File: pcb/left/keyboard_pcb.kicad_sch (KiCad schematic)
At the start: 27 parts, among them J1 TRRS, K00 KEYSW, K01 KEYSW, K02 KEYSW, K03 KEYSW, K04 KEYSW, K05 KEYSW, K10 KEYSW, K11 KEYSW, K12 KEYSW, K13 KEYSW, K14 KEYSW, K15 KEYSW, K20 KEYSW, K21 KEYSW, K22 KEYSW, K23 KEYSW, K24 KEYSW, K25 KEYSW, K30 KEYSW, K31 KEYSW, K32 KEYSW, U1 Helios

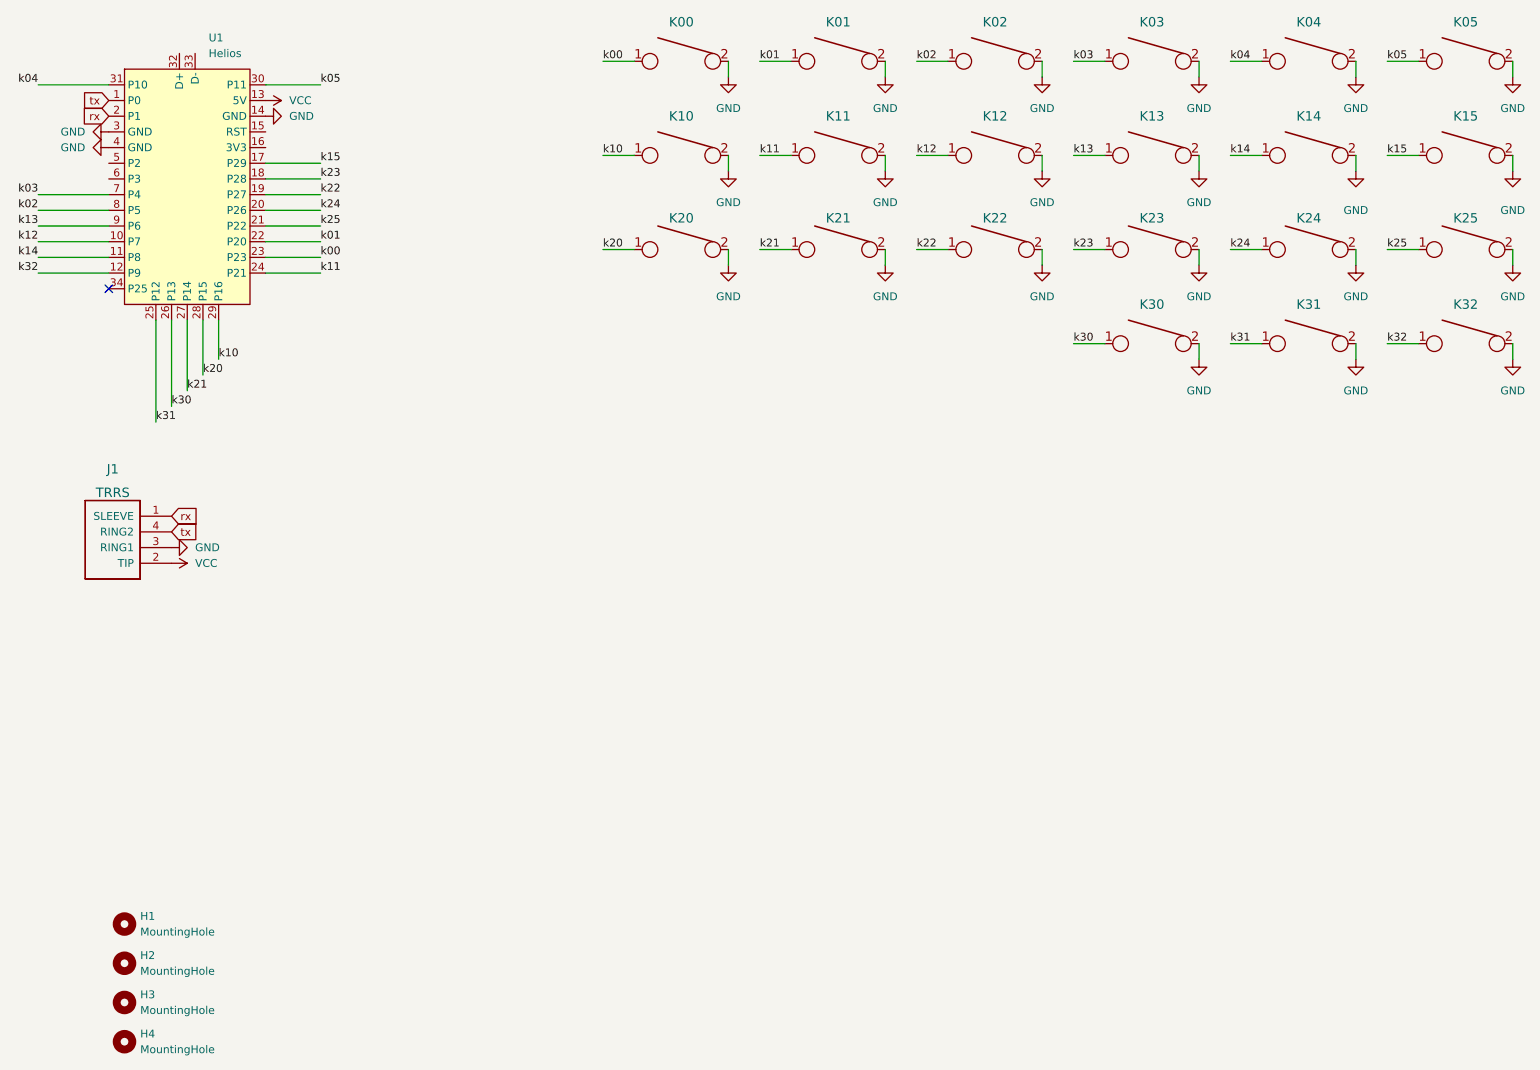
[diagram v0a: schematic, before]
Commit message: Add ground plane. Add reset pins.
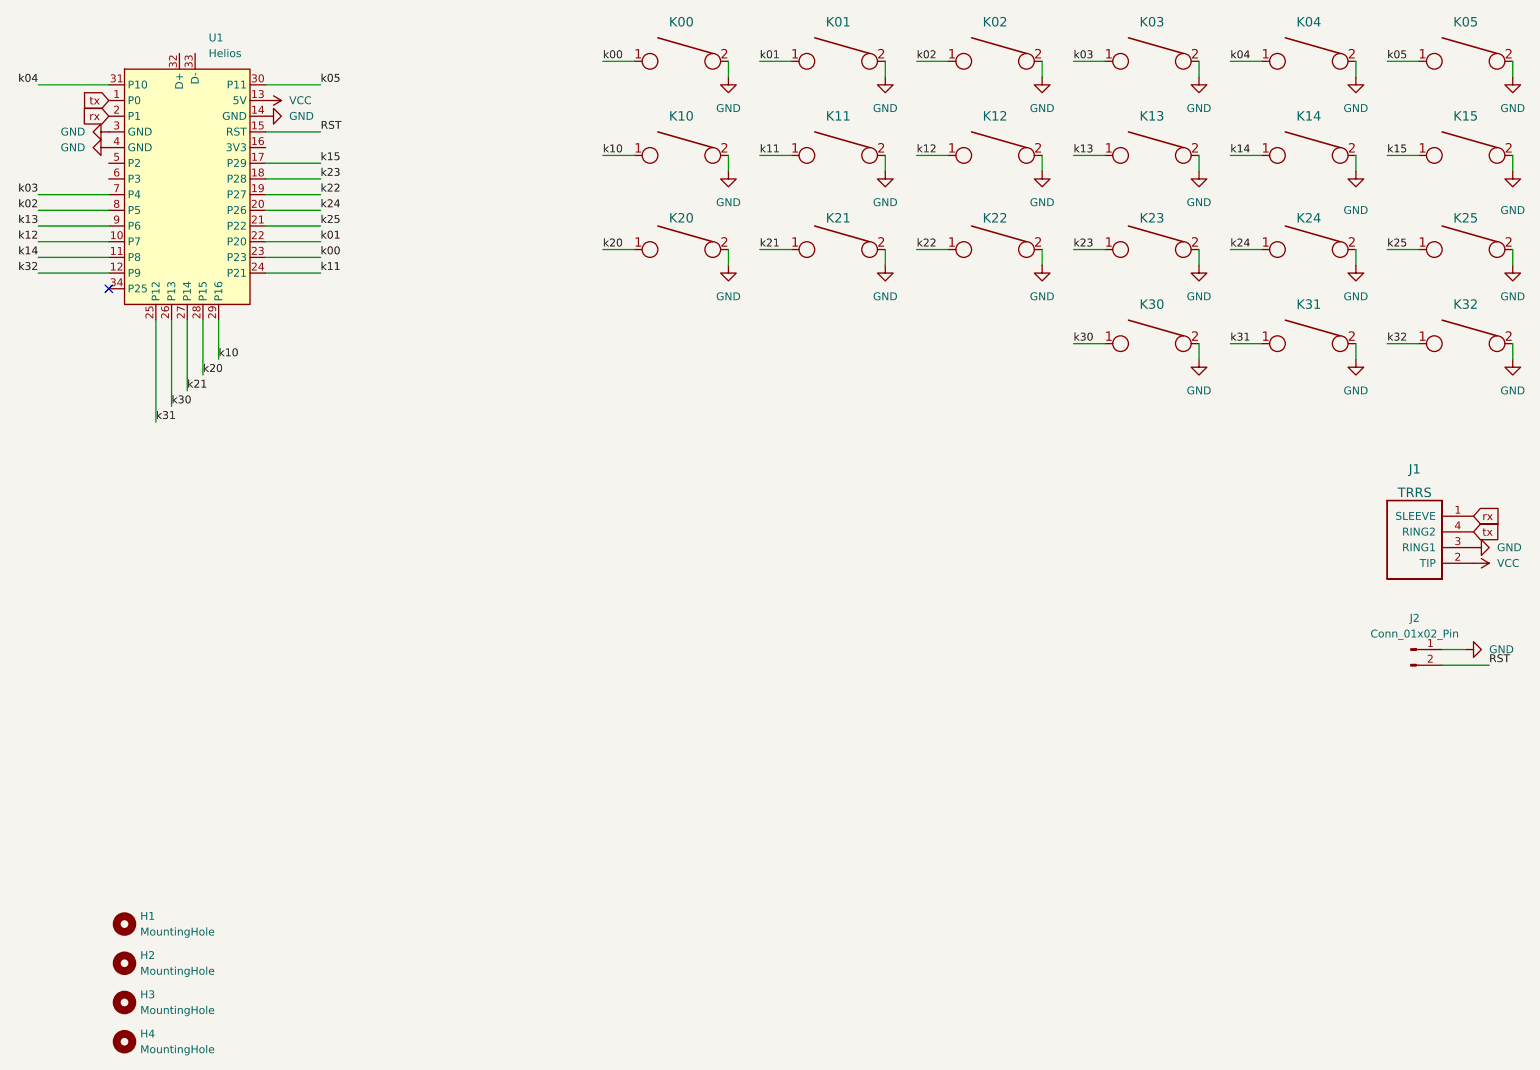
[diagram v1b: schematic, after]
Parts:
- added J2: Conn_01x02_Pin, Connector_PinHeader_2.54mm:PinHeader_1x02_P2.54mm_Vertical, symbol Connector:Conn_01x02_Pin
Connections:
- net GND: now also J2.1 (Pin_1)
- net RST: now reaches U1.15 (RST)
- net RST: now also J2.2 (Pin_2)
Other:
- moved on the sheet: J1
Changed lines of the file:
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@@
 	(wire
 		(pts
+			(xy 69.85 41.91) (xy 78.74 41.91)
+		)
+		(stroke
+			(width 0)
+			(type default)
+		)
+	)
+	(wire
+		(pts
 			(xy 170.18 48.26) (xy 170.18 45.72)
 		)
@@
 	(wire
 		(pts
+			(xy 260.35 125.73) (xy 264.16 125.73)
+		)
+		(stroke
+			(width 0)
+			(type default)
+		)
+	)
+	(wire
+		(pts
 			(xy 33.02 62.23) (xy 44.45 62.23)
 		)
@@
 	(wire
 		(pts
+			(xy 260.35 128.27) (xy 267.97 128.27)
+		)
+		(stroke
+			(width 0)
+			(type default)
+		)
+	)
+	(wire
+		(pts
 			(xy 33.02 54.61) (xy 44.45 54.61)
 		)
@@
 		)
 	)
+	(label "RST"
+		(at 78.74 41.91 0)
+		(fields_autoplaced yes)
+		(effects
+			(font
+				(size 1.27 1.27)
+			)
+			(justify left bottom)
+		)
+	)
 	(label "k24"
 		(at 78.74 54.61 0)
@@
 		)
 	)
+	(label "RST"
+		(at 267.97 128.27 0)
+		(fields_autoplaced yes)
+		(effects
+			(font
+				(size 1.27 1.27)
+			)
+			(justify left bottom)
+		)
+	)
 	(label "k15"
 		(at 78.74 46.99 0)
@@
 	(global_label "rx"
 		(shape input)
-		(at 54.61 104.14 0)
+		(at 265.43 104.14 0)
 		(fields_autoplaced yes)
 		(effects
@@
 		)
 		(property "Intersheetrefs" "${INTERSHEET_REFS}"
-			(at 58.8374 104.2194 0)
+			(at 269.6574 104.2194 0)
 			(effects
 				(font
@@
 	(global_label "tx"
 		(shape input)
-		(at 54.61 106.68 0)
+		(at 265.43 106.68 0)
 		(fields_autoplaced yes)
 		(effects
@@
 		)
 		(property "Intersheetrefs" "${INTERSHEET_REFS}"
-			(at 58.7769 106.7594 0)
+			(at 269.5969 106.7594 0)
 			(effects
 				(font
@@
 	(symbol
 		(lib_id "power:GND")
-		(at 54.61 109.22 90)
+		(at 265.43 109.22 90)
 		(unit 1)
 		(exclude_from_sim no)
@@
 		(fields_autoplaced yes)
 		(property "Reference" "#PWR0126"
-			(at 60.96 109.22 0)
+			(at 271.78 109.22 0)
 			(effects
 				(font
@@
 		)
 		(property "Value" "GND"
-			(at 58.42 109.2199 90)
+			(at 269.24 109.2199 90)
 			(effects
 				(font
@@
 		)
 		(property "Footprint" ""
-			(at 54.61 109.22 0)
+			(at 265.43 109.22 0)
 			(effects
 				(font
@@
 		)
 		(property "Datasheet" ""
-			(at 54.61 109.22 0)
+			(at 265.43 109.22 0)
 			(effects
 				(font
@@
 		)
 		(property "Description" ""
-			(at 54.61 109.22 0)
+			(at 265.43 109.22 0)
 			(effects
 				(font
@@
 	(symbol
 		(lib_id "keebio:TRRS")
-		(at 45.72 101.6 180)
+		(at 256.54 101.6 180)
 		(unit 1)
 		(exclude_from_sim no)
@@
 		(fields_autoplaced yes)
 		(property "Reference" "J1"
-			(at 45.085 96.52 0)
+			(at 255.905 96.52 0)
 			(effects
 				(font
@@
 		)
 		(property "Value" "TRRS"
-			(at 45.085 100.33 0)
+			(at 255.905 100.33 0)
 			(effects
 				(font
@@
 		)
 		(property "Footprint" "Keebio-Parts:TRRS-PJ-320A"
-			(at 41.91 101.6 0)
+			(at 252.73 101.6 0)
 			(effects
 				(font
@@
 		)
 		(property "Datasheet" ""
-			(at 41.91 101.6 0)
+			(at 252.73 101.6 0)
 			(effects
 				(font
@@
 		)
 		(property "Description" ""
-			(at 45.72 101.6 0)
+			(at 256.54 101.6 0)
 			(effects
 				(font
@@
 	)
 	(symbol
+		(lib_id "power:GND")
+		(at 264.16 125.73 90)
+		(unit 1)
+		(exclude_from_sim no)
+		(in_bom yes)
+		(on_board yes)
+		(dnp no)
+		(fields_autoplaced yes)
+		(property "Reference" "#PWR01"
+			(at 270.51 125.73 0)
+			(effects
+				(font
+					(size 1.27 1.27)
+				)
+				(hide yes)
+			)
+		)
+		(property "Value" "GND"
+			(at 267.97 125.7299 90)
+			(effects
+				(font
+					(size 1.27 1.27)
+				)
+				(justify right)
+			)
+		)
+		(property "Footprint" ""
+			(at 264.16 125.73 0)
+			(effects
+				(font
+					(size 1.27 1.27)
+				)
+				(hide yes)
+			)
+		)
+		(property "Datasheet" ""
+			(at 264.16 125.73 0)
+			(effects
+				(font
+					(size 1.27 1.27)
+				)
+				(hide yes)
+			)
+		)
+		(property "Description" ""
+			(at 264.16 125.73 0)
+			(effects
+				(font
+					(size 1.27 1.27)
+				)
+				(hide yes)
+			)
+		)
+		(pin "1"
+		)
+		(instances
+			(project "keyboard_pcb"
+				(path "/9538e4ed-27e6-4c37-b989-9859dc0d49e8"
+					(reference "#PWR01")
+					(unit 1)
+				)
+			)
+		)
+	)
+	(symbol
 		(lib_id "keyboard_parts:KEYSW")
 		(at 264.16 60.96 0)
@@
 	)
 	(symbol
+		(lib_id "Connector:Conn_01x02_Pin")
+		(at 255.27 125.73 0)
+		(unit 1)
+		(exclude_from_sim no)
+		(in_bom yes)
+		(on_board yes)
+		(dnp no)
+		(fields_autoplaced yes)
+		(property "Reference" "J2"
+			(at 255.905 120.65 0)
+			(effects
+				(font
+					(size 1.27 1.27)
+				)
+			)
+		)
+		(property "Value" "Conn_01x02_Pin"
+			(at 255.905 123.19 0)
+			(effects
+				(font
+					(size 1.27 1.27)
+				)
+			)
+		)
+		(property "Footprint" "Connector_PinHeader_2.54mm:PinHeader_1x02_P2.54mm_Vertical"
+			(at 255.27 125.73 0)
+			(effects
+				(font
+					(size 1.27 1.27)
+				)
+				(hide yes)
+			)
+		)
+		(property "Datasheet" "~"
+			(at 255.27 125.73 0)
+			(effects
+				(font
+					(size 1.27 1.27)
+				)
+				(hide yes)
+			)
+		)
+		(property "Description" "Generic connector, single row, 01x02, script generated"
+			(at 255.27 125.73 0)
+			(effects
+				(font
+					(size 1.27 1.27)
+				)
+				(hide yes)
+			)
+		)
+		(pin "1"
+		)
+		(pin "2"
+		)
+		(instances
+			(project ""
+				(path "/9538e4ed-27e6-4c37-b989-9859dc0d49e8"
+					(reference "J2")
+					(unit 1)
+				)
+			)
+		)
+	)
+	(symbol
 		(lib_id "power:GND")
 		(at 144.78 63.5 0)
@@
 	(symbol
 		(lib_id "power:VCC")
-		(at 54.61 111.76 270)
+		(at 265.43 111.76 270)
 		(unit 1)
 		(exclude_from_sim no)
@@
 		(fields_autoplaced yes)
 		(property "Reference" "#PWR0110"
-			(at 50.8 111.76 0)
+			(at 261.62 111.76 0)
 			(effects
 				(font
@@
 		)
 		(property "Value" "VCC"
-			(at 58.42 111.7599 90)
+			(at 269.24 111.7599 90)
 			(effects
 				(font
@@
 		)
 		(property "Footprint" ""
-			(at 54.61 111.76 0)
+			(at 265.43 111.76 0)
 			(effects
 				(font
@@
 		)
 		(property "Datasheet" ""
-			(at 54.61 111.76 0)
+			(at 265.43 111.76 0)
 			(effects
 				(font
@@
 		)
 		(property "Description" ""
-			(at 54.61 111.76 0)
+			(at 265.43 111.76 0)
 			(effects
 				(font

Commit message: Rotate TRRS jack. Replace reset pins by reset button.
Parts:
- J2: footprint Connector_PinHeader_2.54mm:PinHeader_1x02_P2.54mm_Vertical -> PCM_marbastlib-various:SW_SKHLLCA010
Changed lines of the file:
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@@
 			)
 		)
-		(property "Footprint" "Connector_PinHeader_2.54mm:PinHeader_1x02_P2.54mm_Vertical"
+		(property "Footprint" "PCM_marbastlib-various:SW_SKHLLCA010"
 			(at 255.27 125.73 0)
 			(effects
